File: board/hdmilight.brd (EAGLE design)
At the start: 68.5 x 68.6 mm, 73 parts, among them IC1 REG1117, IC2 REG1117, J1 POWER_JACKPTH, Q1 28.6363MHz

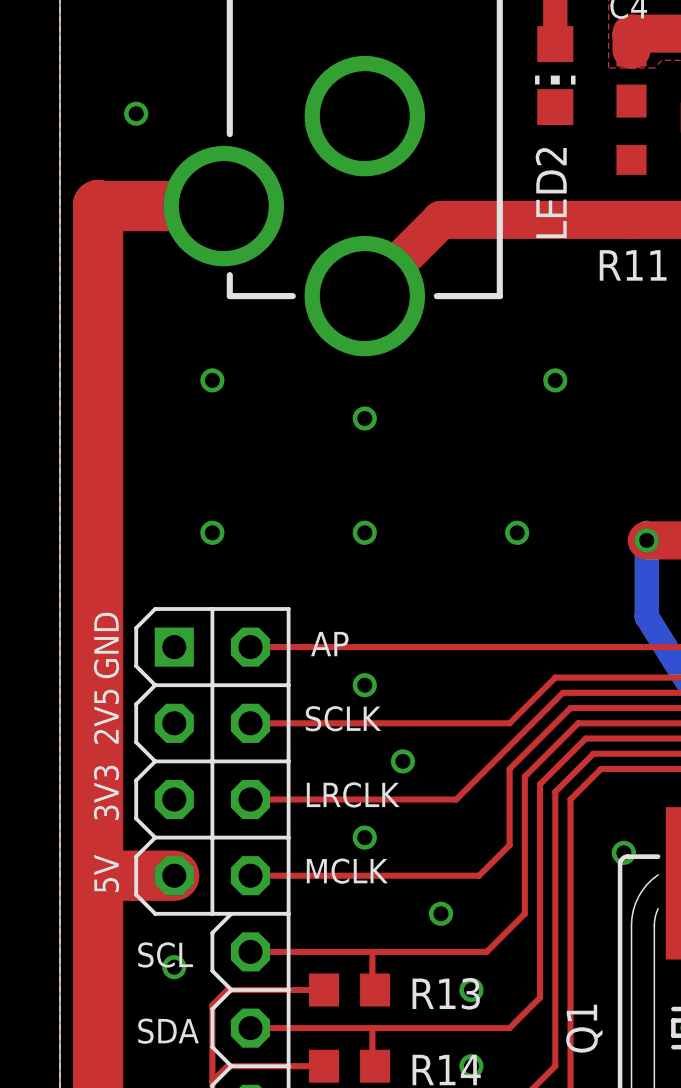
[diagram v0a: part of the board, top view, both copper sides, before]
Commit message: fixed DC plug VCC/GND connection
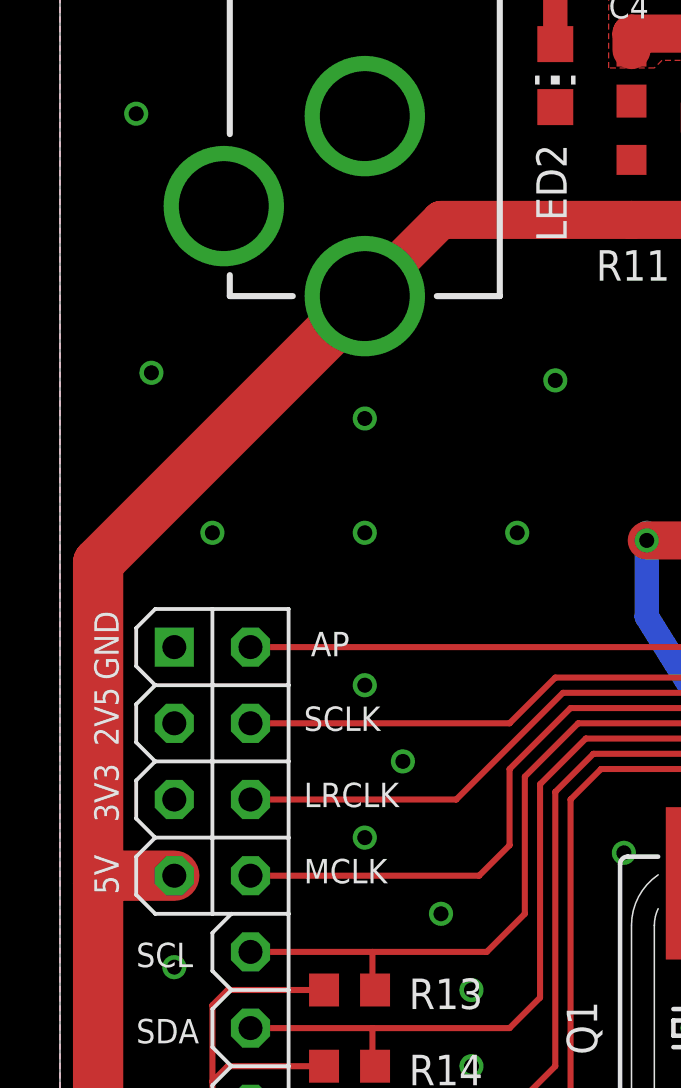
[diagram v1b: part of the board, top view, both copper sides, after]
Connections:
- removed net N$17: F1.1, J1.PWR, R11.1
- net +5V: now also F1.1, J1.PWR, R11.1; no longer J1.GNDBREAK
- net GND: now also J1.GNDBREAK
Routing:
- net N$17: track 15.9 -> 0.00 mm
- net +5V: track 52.1 -> 64.4 mm
